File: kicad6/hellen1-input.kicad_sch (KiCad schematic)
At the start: 57 parts

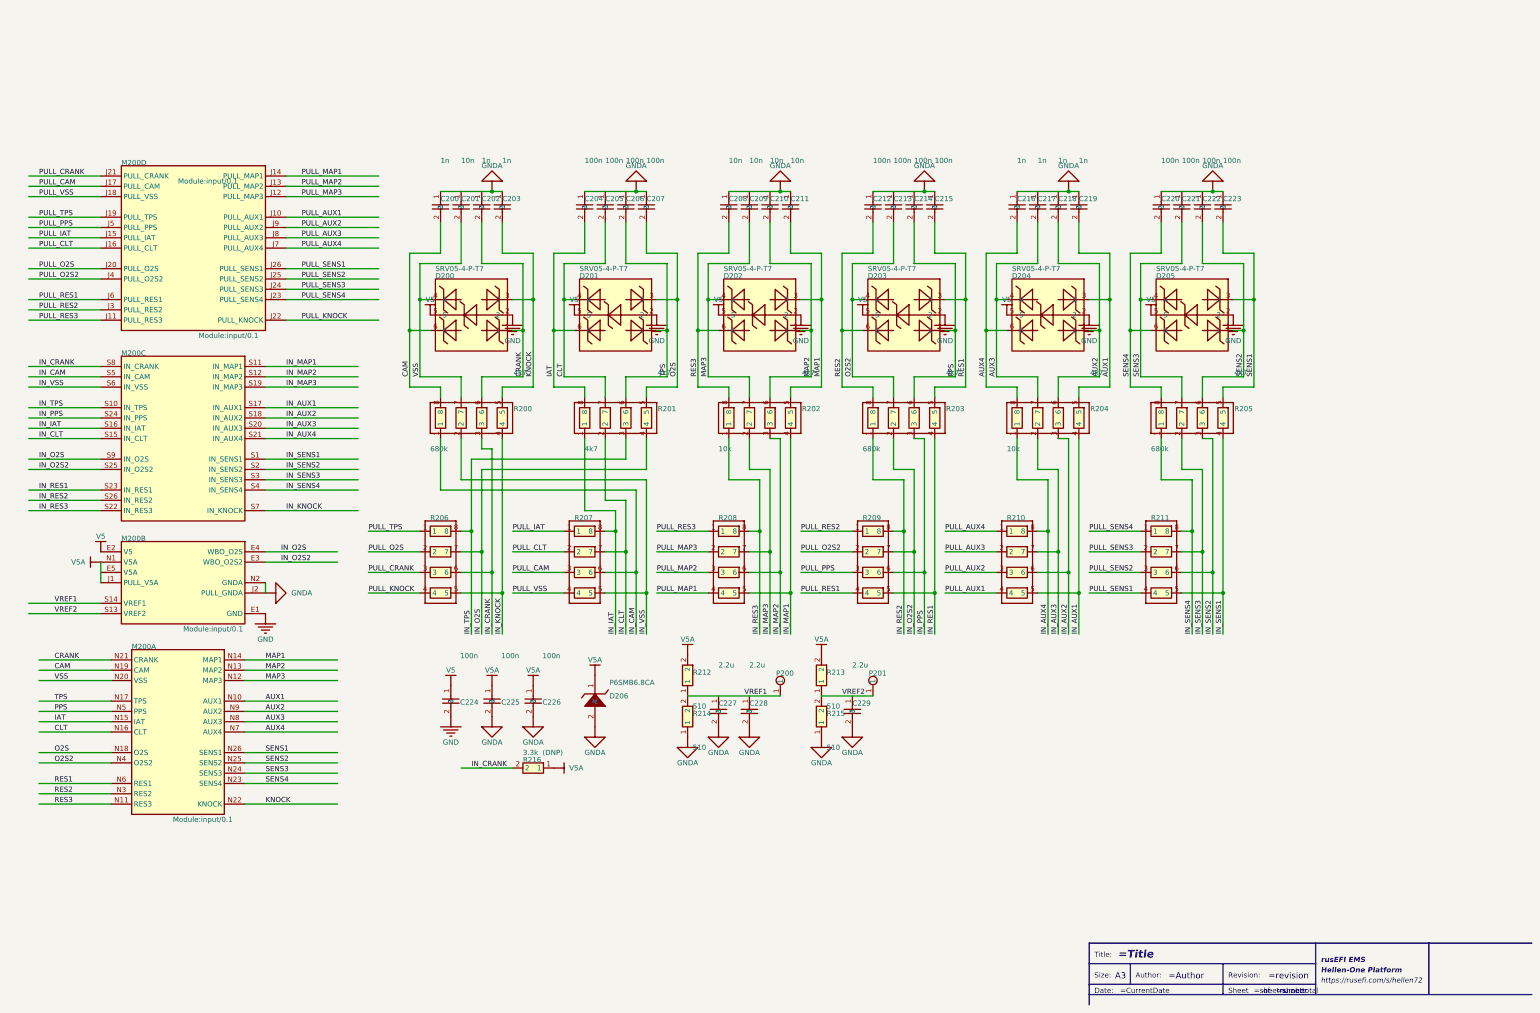
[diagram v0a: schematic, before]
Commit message: move kicad src files into a separate folder
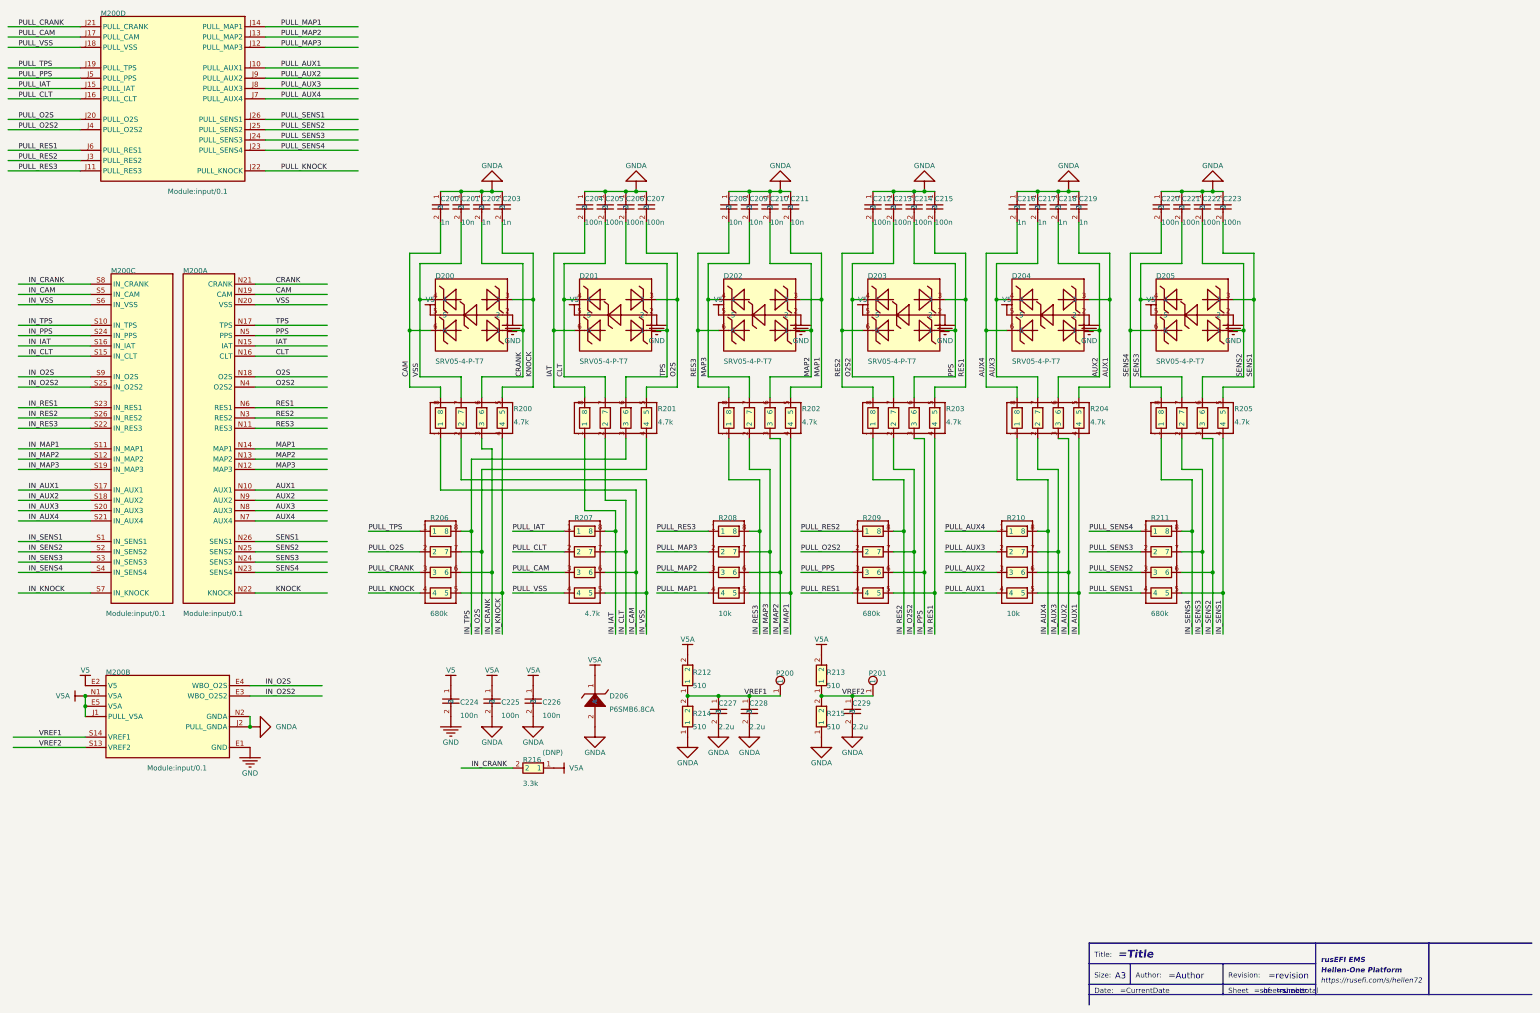
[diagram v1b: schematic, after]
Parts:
- C200, C202, C203, C216, C217, C218, C219: value ~ -> 1n; Comment 1n -> (none)
- C201, C208, C209, C210, C211: value ~ -> 10n; Comment 10n -> (none)
- C204, C205, C206, C207, C212, C213, C214, C215, C220, C221, C222, C223, C224, C225, C226: value ~ -> 100n; Comment 100n -> (none)
- C227, C228, C229: value ~ -> 2.2u; Comment 2.2u -> (none)
- D200, D201, D202, D203, D204, D205: value ~ -> SRV05-4-P-T7; Comment SRV05-4-P-T7 -> (none)
- D206: value ~ -> P6SMB6.8CA; Comment P6SMB6.8CA -> (none)
- M200: value ~ -> Module:input/0.1; Comment Module:input/0.1 -> (none)
- P200: value ~ -> Vref1; Comment Vref1 -> (none)
- P201: value ~ -> Vref2; Comment Vref2 -> (none)
- R200, R201, R202, R203, R204, R205, R207: value ~ -> 4.7k; Comment 4k7 -> (none)
- R206, R209, R211: value ~ -> 680k; Comment 680k -> (none)
- R208, R210: value ~ -> 10k; Comment 10k -> (none)
- R212, R213, R214, R215: value ~ -> 510; Comment 510 -> (none)
- R216: value ~ -> 3.3k; Comment 3.3k -> (none)
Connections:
- net GNDA: now also C201.1, C202.1, C205.1, C206.1, C209.1, C210.1, C213.1, C214.1, C217.1, C218.1, C221.1, C222.1
- net V5A: now also M200.E5 (V5A)
- net VREF1: now also C227.1, C228.1
- net VREF2: now also C229.1
